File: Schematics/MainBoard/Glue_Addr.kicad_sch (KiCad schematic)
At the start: 35 parts, among them IC1 ATF1508AS-7AX100, J1 Conn_02x05_Odd_Even, J15 Conn_01x06, J16 Conn_01x03, J18 Conn_01x03, X1 16MHz

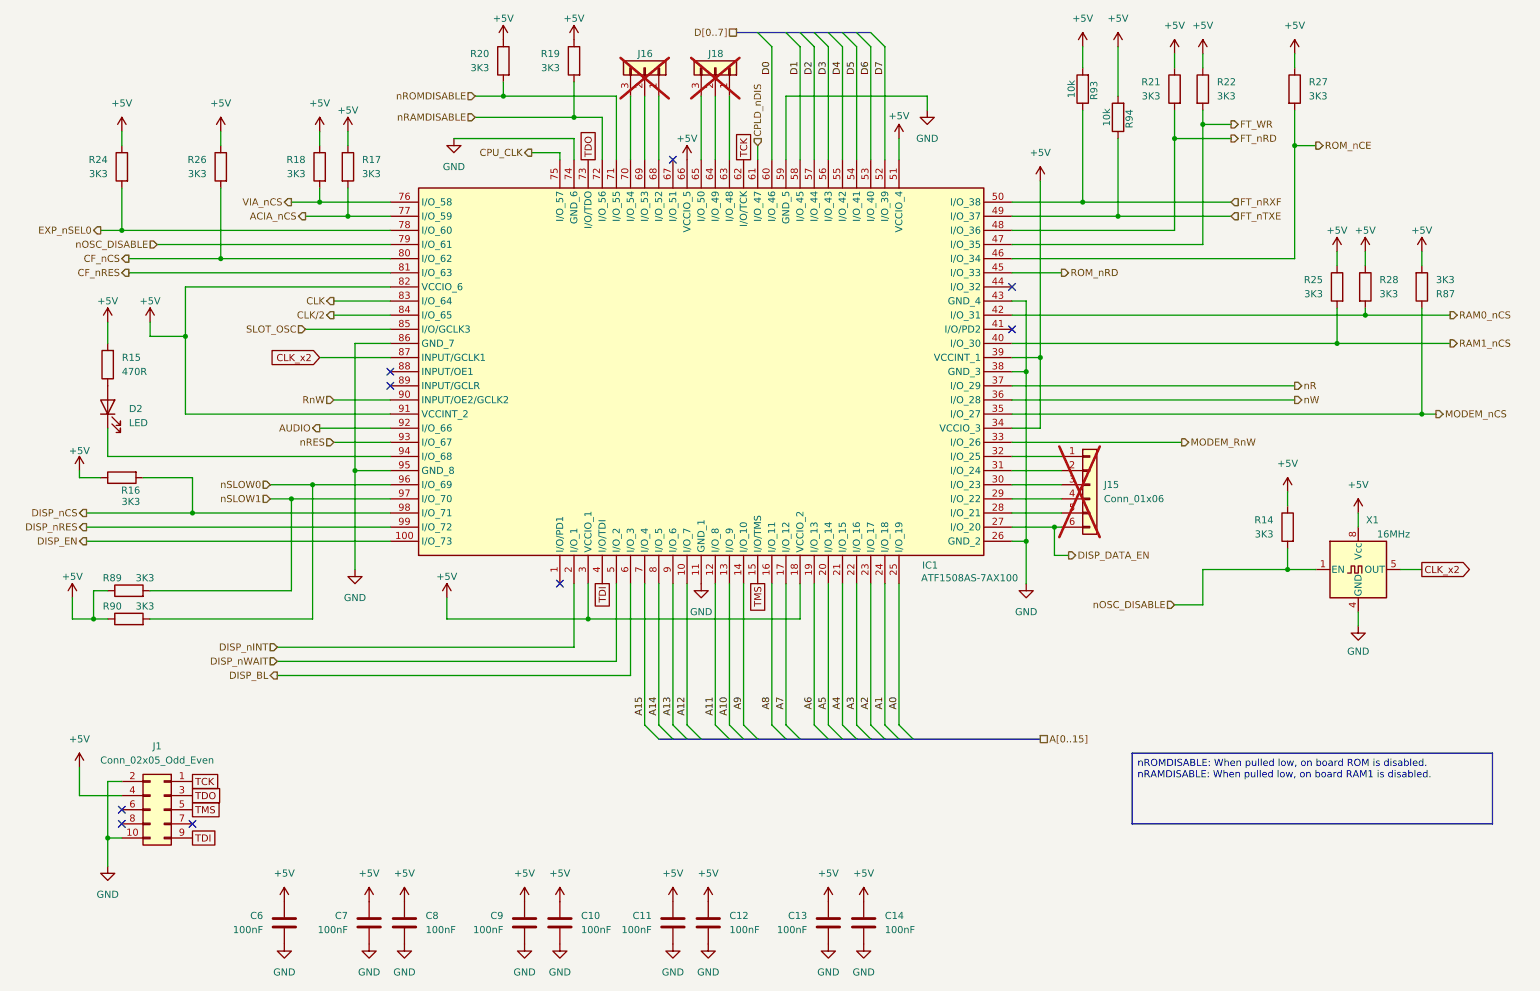
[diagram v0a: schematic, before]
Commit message: Move to a single board for everything (keyboard and main board)
Aim is to save height
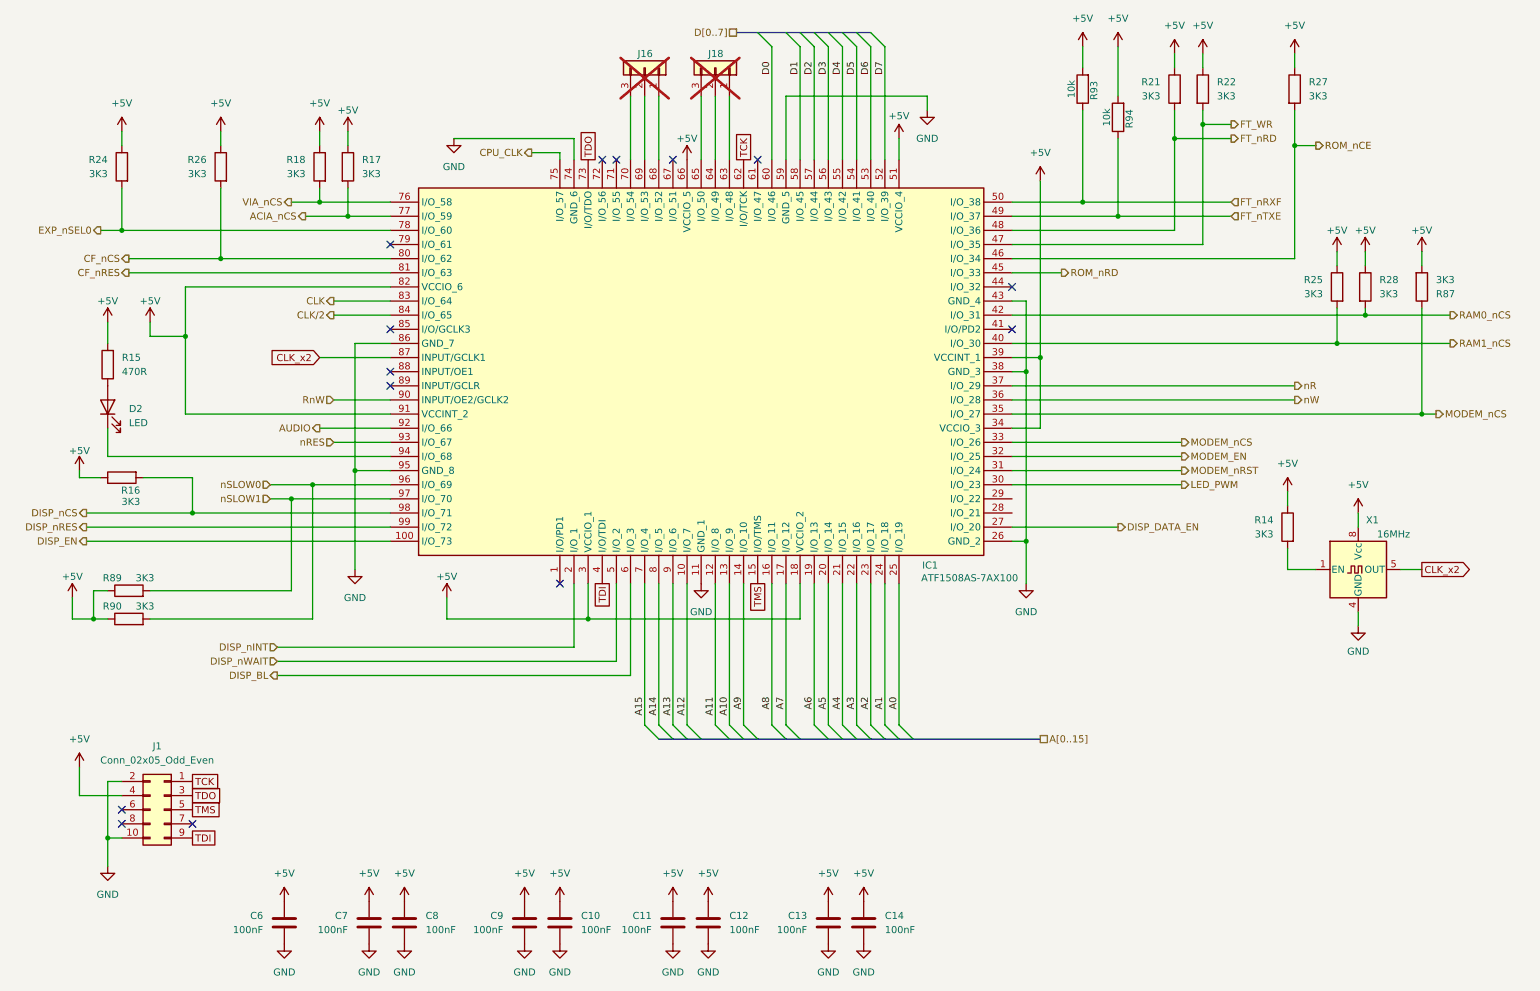
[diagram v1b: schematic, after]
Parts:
- removed J15: Conn_01x06, Connector_PinHeader_1.00mm:PinHeader_1x06_P1.00mm_Vertical_SMD_Pin1Left, symbol Connector_Generic:Conn_01x06
- removed R19, R20: 3K3, Resistor_SMD:R_0402_1005Metric, symbol Device:R
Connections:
- net MODEM_RnW is gone; now on net MODEM_nCS: IC1.33 (I/O_26)
- net LED_PWM: now reaches IC1.30 (I/O_23)
- net MODEM_nRST: now reaches IC1.31 (I/O_24)
- net MODEM_EN: now reaches IC1.32 (I/O_25)
- net CPLD_nDIS: no longer names the net of IC1.61 (I/O_47)
- net SLOT_OSC: no longer names the net of IC1.85 (I/O/GCLK3)
- net nOSC_DISABLE: no longer names the net of R14.2, X1.1 (EN)
- net nOSC_DISABLE: no longer IC1.79 (I/O_61)
- net nRAMDISABLE: no longer names the net of IC1.72 (I/O_56)
- net nROMDISABLE: no longer names the net of IC1.71 (I/O_55)
- no-connect marks 9 -> 14

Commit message: Work on PCB
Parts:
- removed R14: 3K3, Resistor_SMD:R_0402_1005Metric, symbol Device:R
- C11, C12, C13, C14, C6, C7, C8, C9: footprint Capacitor_SMD:C_0603_1608Metric -> Capacitor_SMD:C_0402_1005Metric
- J1: footprint Connector_PinHeader_2.54mm:PinHeader_2x05_P2.54mm_Vertical -> Connector_PinHeader_2.54mm:PinHeader_2x05_P2.54mm_Horizontal
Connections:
- net A0: now also IC1.19 (I/O_13); no longer IC1.25 (I/O_19)
- net A1: now also IC1.20 (I/O_14); no longer IC1.24 (I/O_18)
- net A2: now also IC1.21 (I/O_15); no longer IC1.23 (I/O_17)
- net A4: now also IC1.23 (I/O_17); no longer IC1.21 (I/O_15)
- net A5: now also IC1.24 (I/O_18); no longer IC1.20 (I/O_14)
- net A6: now also IC1.25 (I/O_19); no longer IC1.19 (I/O_13)
- no-connect marks 14 -> 15
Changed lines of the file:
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@@
 	)
 	(no_connect
+		(at 247.65 119.38)
+	)
+	(no_connect
 		(at 193.04 68.58)
 	)
@@
 	(wire
 		(pts
-			(xy 172.72 147.32) (xy 172.72 121.92)
+			(xy 157.48 147.32) (xy 157.48 121.92)
 		)
 		(stroke
@@
 	(wire
 		(pts
-			(xy 167.64 147.32) (xy 167.64 121.92)
+			(xy 162.56 147.32) (xy 162.56 121.92)
 		)
 		(stroke
@@
 	(wire
 		(pts
-			(xy 157.48 121.92) (xy 157.48 147.32)
+			(xy 172.72 121.92) (xy 172.72 147.32)
 		)
 		(stroke
@@
 	(wire
 		(pts
-			(xy 247.65 119.38) (xy 242.57 119.38)
-		)
-		(stroke
-			(width 0)
-			(type default)
-		)
-	)
-	(wire
-		(pts
 			(xy 162.56 25.4) (xy 162.56 45.72)
 		)
@@
 	(wire
 		(pts
-			(xy 242.57 119.38) (xy 242.57 115.57)
-		)
-		(stroke
-			(width 0)
-			(type default)
-		)
-	)
-	(wire
-		(pts
 			(xy 144.78 121.92) (xy 144.78 147.32)
 		)
@@
 	(wire
 		(pts
-			(xy 162.56 147.32) (xy 162.56 121.92)
+			(xy 167.64 147.32) (xy 167.64 121.92)
 		)
 		(stroke
@@
 	(wire
 		(pts
-			(xy 160.02 147.32) (xy 160.02 121.92)
+			(xy 170.18 147.32) (xy 170.18 121.92)
 		)
 		(stroke
@@
 	(wire
 		(pts
-			(xy 242.57 105.41) (xy 242.57 107.95)
-		)
-		(stroke
-			(width 0)
-			(type default)
-		)
-	)
-	(wire
-		(pts
 			(xy 30.48 74.93) (xy 30.48 78.74)
 		)
@@
 	(wire
 		(pts
-			(xy 170.18 147.32) (xy 170.18 121.92)
+			(xy 160.02 147.32) (xy 160.02 121.92)
 		)
 		(stroke
@@
 	)
 	(label "A5"
-		(at 160.02 142.24 270)
+		(at 170.18 142.24 270)
 		(effects
 			(font
@@
 	)
 	(label "A1"
-		(at 170.18 142.24 270)
+		(at 160.02 142.24 270)
 		(effects
 			(font
@@
 	)
 	(label "A4"
-		(at 162.56 142.24 270)
+		(at 167.64 142.24 270)
 		(effects
 			(font
@@
 	)
 	(label "A2"
-		(at 167.64 142.24 270)
+		(at 162.56 142.24 270)
 		(effects
 			(font
@@
 	)
 	(label "A6"
-		(at 157.48 142.24 270)
+		(at 172.72 142.24 270)
 		(effects
 			(font
@@
 	)
 	(label "A0"
-		(at 172.72 142.24 270)
+		(at 157.48 142.24 270)
 		(effects
 			(font
@@
 			)
 		)
-		(property "Footprint" "Capacitor_SMD:C_0603_1608Metric"
+		(property "Footprint" "Capacitor_SMD:C_0402_1005Metric"
 			(at 139.3952 186.69 0)
 			(effects
@@
 			)
 		)
-		(property "Footprint" "Connector_PinHeader_2.54mm:PinHeader_2x05_P2.54mm_Vertical"
+		(property "Footprint" "Connector_PinHeader_2.54mm:PinHeader_2x05_P2.54mm_Horizontal"
 			(at 40.64 162.56 0)
 			(effects
@@
 			)
 		)
-		(property "Footprint" "Capacitor_SMD:C_0603_1608Metric"
+		(property "Footprint" "Capacitor_SMD:C_0402_1005Metric"
 			(at 131.1148 186.69 0)
 			(effects
@@
 			)
 		)
-		(property "Footprint" "Capacitor_SMD:C_0603_1608Metric"
+		(property "Footprint" "Capacitor_SMD:C_0402_1005Metric"
 			(at 159.0548 186.69 0)
 			(effects
@@
 			)
 		)
-		(property "Footprint" "Capacitor_SMD:C_0603_1608Metric"
+		(property "Footprint" "Capacitor_SMD:C_0402_1005Metric"
 			(at 104.4448 186.69 0)
 			(effects
@@
 			)
 		)
-		(property "Footprint" "Capacitor_SMD:C_0603_1608Metric"
+		(property "Footprint" "Capacitor_SMD:C_0402_1005Metric"
 			(at 76.5048 186.69 0)
 			(effects
@@
 			)
 		)
-		(property "Footprint" "Capacitor_SMD:C_0603_1608Metric"
+		(property "Footprint" "Capacitor_SMD:C_0402_1005Metric"
 			(at 61.2648 186.69 0)
 			(effects
@@
 			)
 		)
-		(property "Footprint" "Capacitor_SMD:C_0603_1608Metric"
+		(property "Footprint" "Capacitor_SMD:C_0402_1005Metric"
 			(at 84.7852 186.69 0)
 			(effects
@@
 	)
 	(symbol
-		(lib_id "Device:R")
-		(at 242.57 111.76 0)
-		(mirror y)
-		(unit 1)
-		(exclude_from_sim no)
-		(in_bom yes)
-		(on_board yes)
-		(dnp no)
-		(fields_autoplaced yes)
-		(property "Reference" "R14"
-			(at 240.03 110.4899 0)
-			(effects
-				(font
-					(size 1.27 1.27)
-				)
-				(justify left)
-			)
-		)
-		(property "Value" "3K3"
-			(at 240.03 113.0299 0)
-			(effects
-				(font
-					(size 1.27 1.27)
-				)
-				(justify left)
-			)
-		)
-		(property "Footprint" "Resistor_SMD:R_0402_1005Metric"
-			(at 244.348 111.76 90)
-			(effects
-				(font
-					(size 1.27 1.27)
-				)
-				(hide yes)
-			)
-		)
-		(property "Datasheet" "~"
-			(at 242.57 111.76 0)
-			(effects
-				(font
-					(size 1.27 1.27)
-				)
-				(hide yes)
-			)
-		)
-		(property "Description" ""
-			(at 242.57 111.76 0)
-			(effects
-				(font
-					(size 1.27 1.27)
-				)
-			)
-		)
-		(property "LCSC" "C25890"
-			(at 242.57 111.76 0)
-			(effects
-				(font
-					(size 1.27 1.27)
-				)
-				(hide yes)
-			)
-		)
-		(pin "1"
-		)
-		(pin "2"
-		)
-		(instances
-			(project "LT6502"
-				(path "/a2243a34-697c-4939-97f7-df548e421864/d5afc5d6-c446-466d-ac54-32ad85bd9dec"
-					(reference "R14")
-					(unit 1)
-				)
-			)
-		)
-	)
-	(symbol
 		(lib_id "power:+5V")
 		(at 38.1 74.93 0)
@@
 			)
 		)
-		(property "Footprint" "Capacitor_SMD:C_0603_1608Metric"
+		(property "Footprint" "Capacitor_SMD:C_0402_1005Metric"
 			(at 167.3352 186.69 0)
 			(effects
@@
 					(unit 1)
 				)
-			)
-		)
-	)
-	(symbol
-		(lib_id "power:+5V")
-		(at 242.57 105.41 0)
-		(mirror y)
-		(unit 1)
-		(exclude_from_sim no)
-		(in_bom yes)
-		(on_board yes)
-		(dnp no)
-		(fields_autoplaced yes)
-		(property "Reference" "#PWR040"
-			(at 242.57 109.22 0)
-			(effects
-				(font
-					(size 1.27 1.27)
-				)
-				(hide yes)
-			)
-		)
-		(property "Value" "+5V"
-			(at 242.57 100.33 0)
-			(effects
-				(font
-					(size 1.27 1.27)
-				)
-			)
-		)
-		(property "Footprint" ""
-			(at 242.57 105.41 0)
-			(effects
-				(font
-					(size 1.27 1.27)
-				)
-				(hide yes)
-			)
-		)
-		(property "Datasheet" ""
-			(at 242.57 105.41 0)
-			(effects
-				(font
-					(size 1.27 1.27)
-				)
-				(hide yes)
-			)
-		)
-		(property "Description" ""
-			(at 242.57 105.41 0)
-			(effects
-				(font
-					(size 1.27 1.27)
-				)
-			)
-		)
-		(pin "1"
-		)
-		(instances
-			(project "LT6502"
-				(path "/a2243a34-697c-4939-97f7-df548e421864/d5afc5d6-c446-466d-ac54-32ad85bd9dec"
-					(reference "#PWR040")
-					(unit 1)
-				)

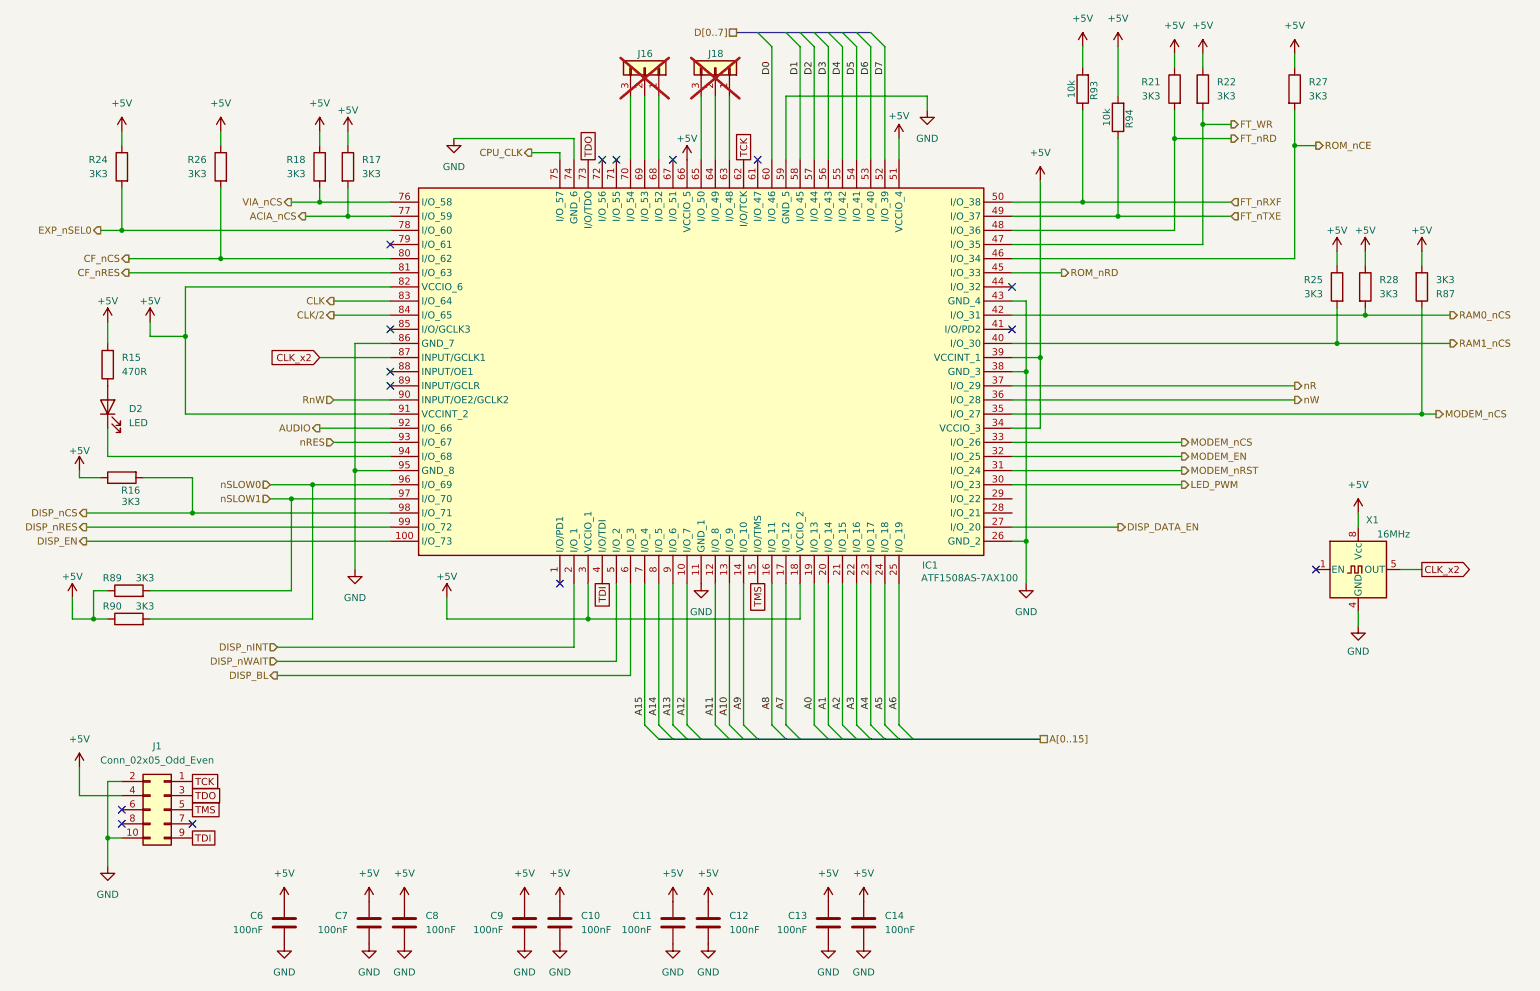
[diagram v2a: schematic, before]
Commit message: Work on PCB routing, added SwinSID
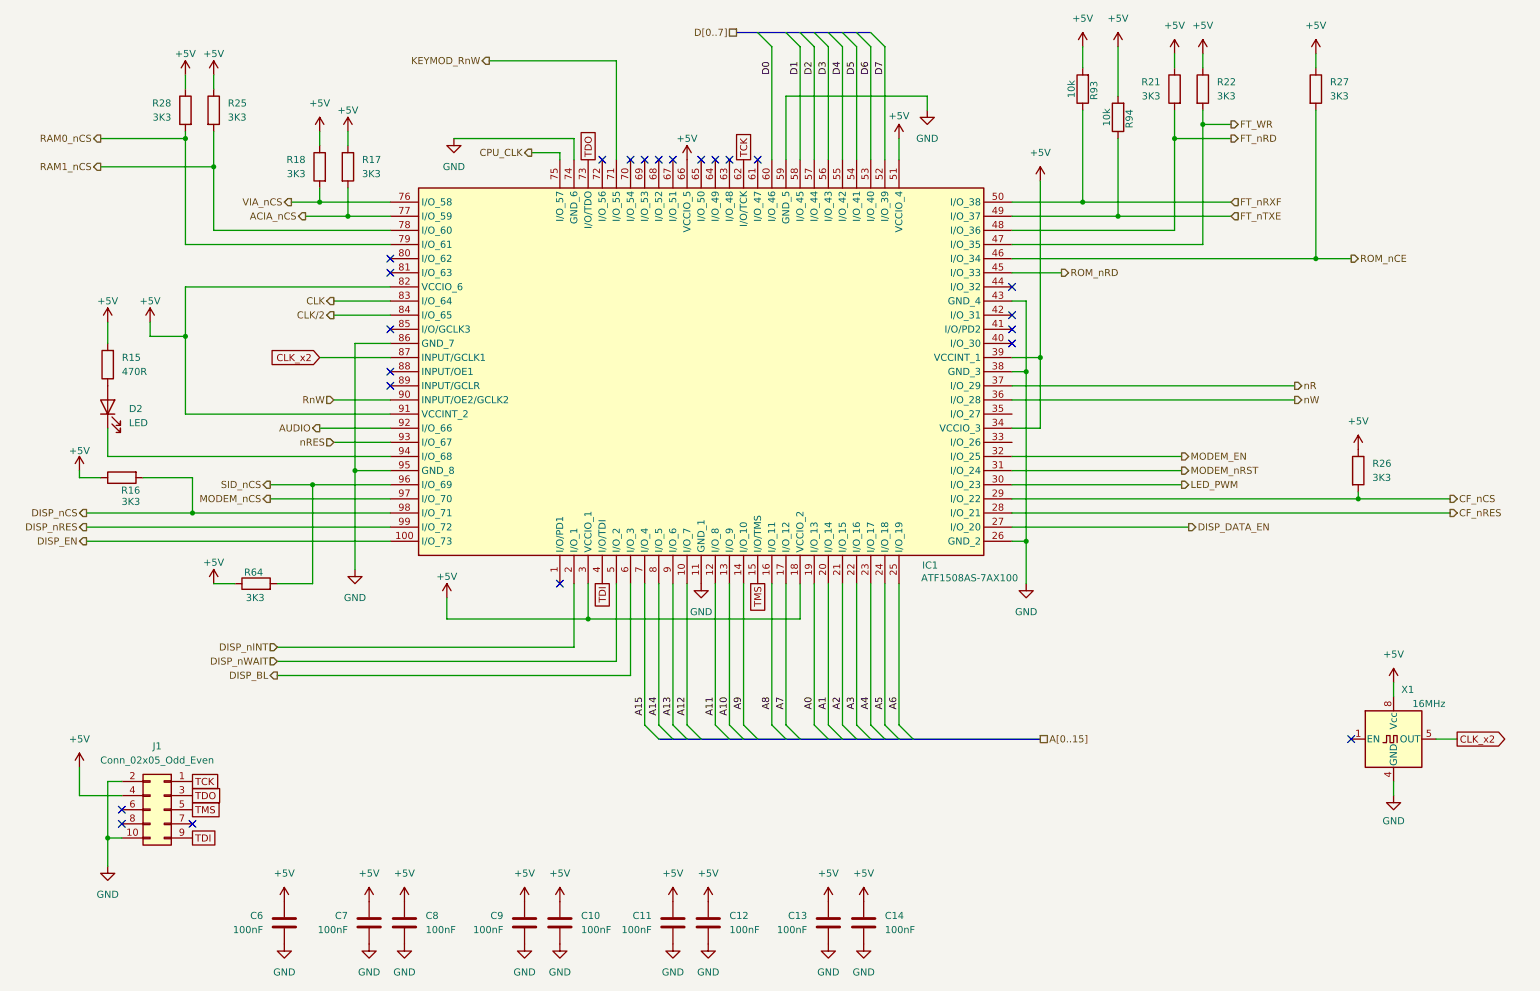
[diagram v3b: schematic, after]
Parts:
- removed J16, J18: Conn_01x03, Connector_PinHeader_1.00mm:PinHeader_1x03_P1.00mm_Vertical_SMD_Pin1Left, symbol Connector_Generic:Conn_01x03
- removed R24, R87, R89, R90: 3K3, Resistor_SMD:R_0402_1005Metric, symbol Device:R
- added R64: 3K3, Resistor_SMD:R_0402_1005Metric, symbol Device:R
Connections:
- net EXP_nSEL0 is gone; now on net RAM1_nCS: IC1.78 (I/O_60)
- net nSLOW1 is gone; now on net MODEM_nCS: IC1.97 (I/O_70)
- net +5V: now also R64.1
- net CF_nCS: now also IC1.29 (I/O_22); no longer IC1.80 (I/O_62)
- net CF_nRES: now also IC1.28 (I/O_21); no longer IC1.81 (I/O_63)
- net MODEM_nCS: no longer IC1.33 (I/O_26), IC1.35 (I/O_27)
- net RAM0_nCS: now also IC1.79 (I/O_61); no longer IC1.42 (I/O_31)
- net RAM1_nCS: no longer IC1.40 (I/O_30)
- net KEYMOD_RnW: now reaches IC1.71 (I/O_55)
- net nSLOW0 renamed SID_nCS
- net SID_nCS: now also R64.2
- no-connect marks 15 -> 23
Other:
- moved on the sheet: R25, R26, R27, R28, X1
